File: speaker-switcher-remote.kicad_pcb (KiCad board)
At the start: 2 copper layers, 92 x 60 mm, 31 parts, among them M1 arduino-nano, Q1 2N2222, Q2 TIP31C, U1 LM7805_TO220

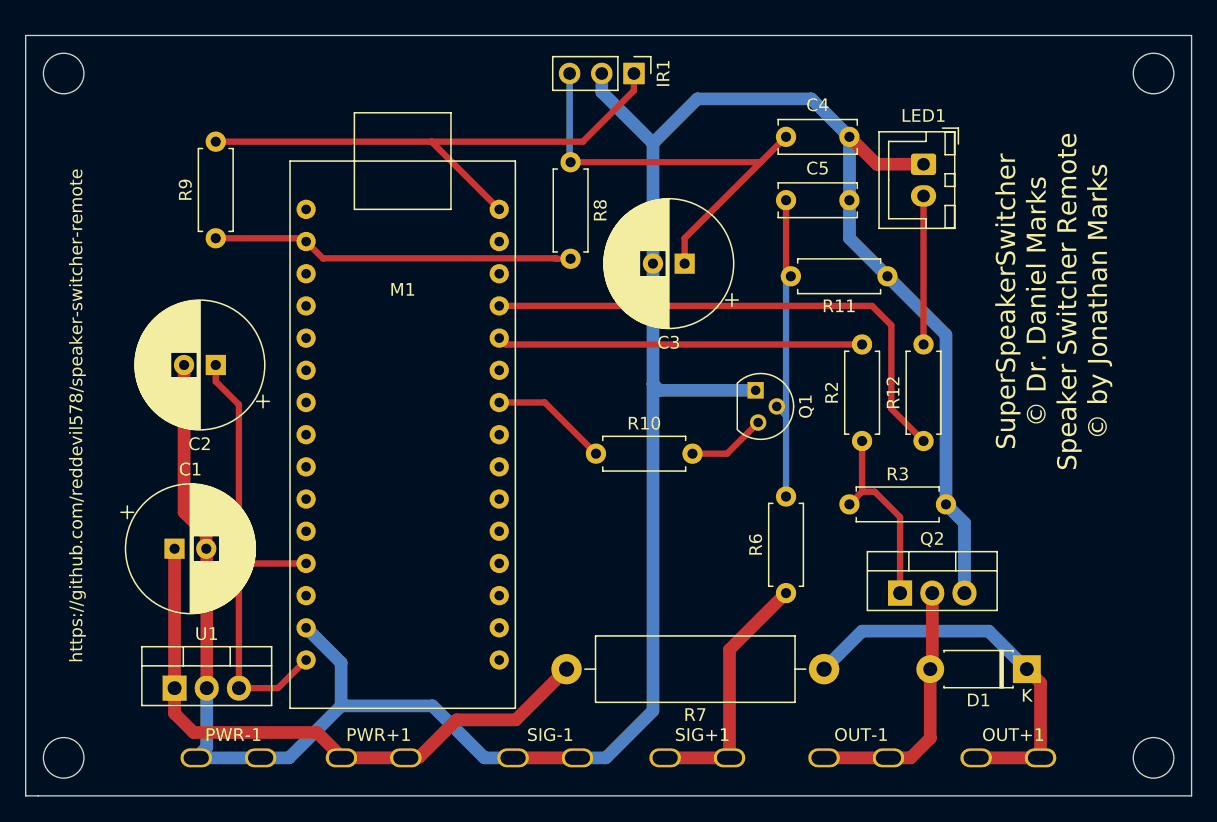
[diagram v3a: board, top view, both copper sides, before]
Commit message: Updated w/PNP output stage
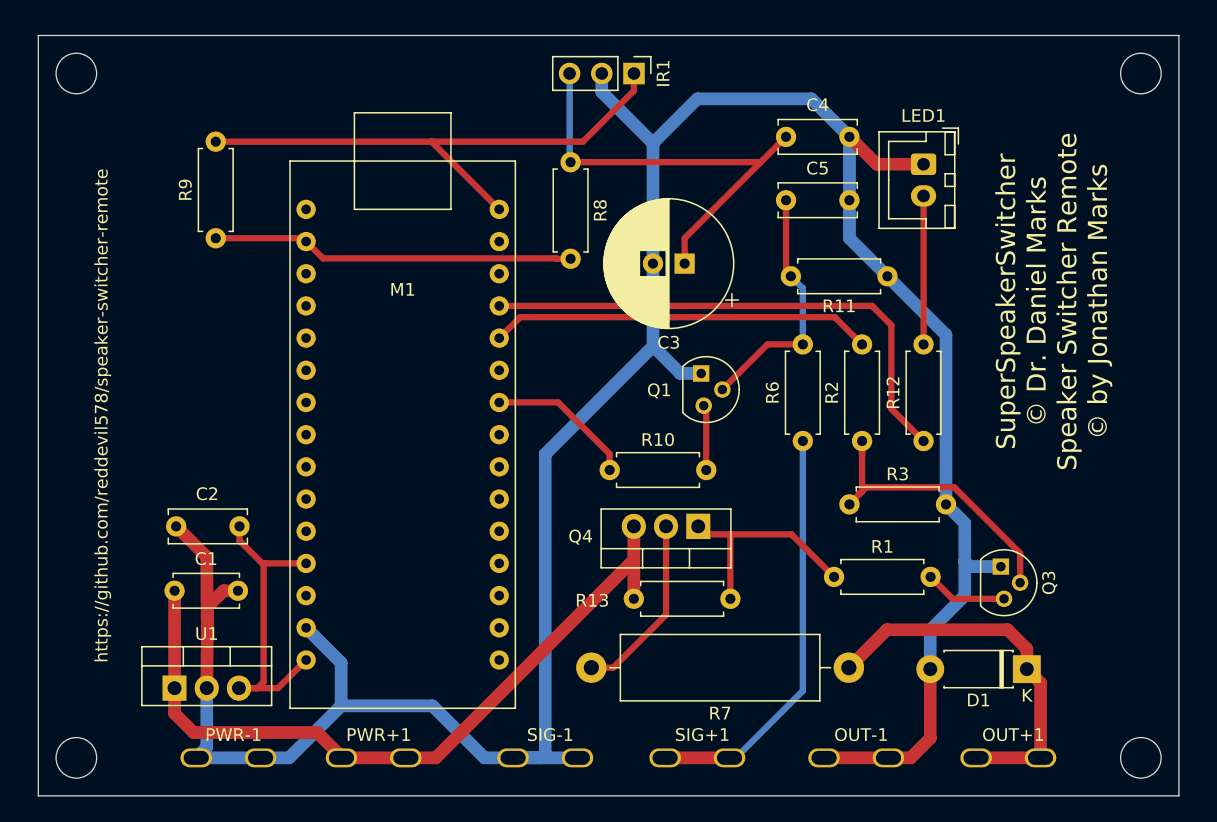
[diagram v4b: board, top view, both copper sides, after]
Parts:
- removed Q2: TIP31C, Package_TO_SOT_THT:TO-220-3_Vertical
- added Q3: 2N2222, Package_TO_SOT_THT:TO-92, F.Cu at (179.4, 110.4)
- added Q4: Q_PNP_BCE, Package_TO_SOT_THT:TO-220-3_Vertical, F.Cu at (155.3, 107.2)
- added R1: 2.2k, Resistor_THT:R_Axial_DIN0207_L6.3mm_D2.5mm_P7.62mm_Horizontal, F.Cu at (166.0, 111.2)
- added R13: 100k, Resistor_THT:R_Axial_DIN0207_L6.3mm_D2.5mm_P7.62mm_Horizontal, F.Cu at (150.2, 113.0)
- C1: footprint Capacitor_THT:CP_Radial_D10.0mm_P2.50mm -> Capacitor_THT:C_Disc_D5.0mm_W2.5mm_P5.00mm
- C2: footprint Capacitor_THT:CP_Radial_D10.0mm_P2.50mm -> Capacitor_THT:C_Disc_D6.0mm_W2.5mm_P5.00mm
- R12: value 150 -> 2.2k
- moved C2 12.9 mm to (119.1, 107.2)
- moved R6 12.1 mm to (163.6, 100.5)
- moved Q1 4.50 mm to (156.0, 95.2)
- moved C1 3.31 mm to (114.0, 112.3)
- moved R7 1.96 mm to (167.2, 118.4)
- moved R10 1.69 mm to (148.3, 102.8)
- moved REF** 1.00 mm to (106.2, 125.5)
- moved REF** 1.00 mm to (190.2, 125.5)
- moved REF** 1.00 mm to (190.2, 71.5)
- moved REF** 1.00 mm to (106.2, 71.5)
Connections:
- D1 pad 2: Net-(D1-Pad2) -> GNDREF
- M1 pad 1: Net-(M1-Pad1) -> (no net)
- M1 pad 10: Net-(M1-Pad10) -> (no net)
- M1 pad 11: Net-(M1-Pad11) -> (no net)
- M1 pad 13: Net-(M1-Pad13) -> (no net)
- M1 pad 17: Net-(M1-Pad17) -> (no net)
- M1 pad 18: Net-(M1-Pad18) -> (no net)
- M1 pad 21: Net-(M1-Pad21) -> (no net)
- M1 pad 23: Net-(M1-Pad23) -> (no net)
- M1 pad 24: Net-(M1-Pad24) -> (no net)
- M1 pad 25: Net-(M1-Pad25) -> (no net)
- M1 pad 26: Net-(M1-Pad26) -> (no net)
- M1 pad 27: Net-(M1-Pad27) -> (no net)
- M1 pad 28: Net-(M1-Pad28) -> (no net)
- M1 pad 29: Net-(M1-Pad29) -> (no net)
- M1 pad 3: Net-(M1-Pad3) -> (no net)
- M1 pad 30: Net-(M1-Pad30) -> (no net)
- M1 pad 4: Net-(M1-Pad4) -> (no net)
- M1 pad 5: Net-(M1-Pad5) -> (no net)
- M1 pad 6: Net-(M1-Pad6) -> (no net)
- M1 pad 7: Net-(M1-Pad7) -> (no net)
- M1 pad 8: Net-(M1-Pad8) -> (no net)
- M1 pad 9: Net-(M1-Pad9) -> (no net)
- OUT-1 pad 1: Net-(D1-Pad2) -> GNDREF
- R7 pad 2: PWR -> Net-(Q4-Pad2)
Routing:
- net Net-(D1-Pad2): track 20.5 -> 0.00 mm
- net Net-(Q4-Pad1): track 0.00 -> 17.2 mm
- net GNDREF: track 205.7 -> 222.0 mm
- net Net-(Q4-Pad2): track 0.00 -> 14.0 mm
- net /+5V: track 37.8 -> 24.8 mm
- net Net-(R6-Pad1): track 19.9 -> 32.8 mm
- net PWR: track 47.5 -> 59.1 mm
- net Net-(Q3-Pad2): track 15.2 -> 24.0 mm
- net Net-(Q3-Pad3): track 0.00 -> 6.51 mm
- net Net-(C5-Pad1): track 25.2 -> 19.8 mm
- net Net-(M1-Pad22): track 9.30 -> 11.7 mm
- net Net-(M1-Pad20): track 28.8 -> 30.2 mm
- net Net-(Q1-Pad3): track 6.20 -> 5.16 mm
- net Net-(D1-Pad1): track 31.0 -> 30.0 mm
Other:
- board size 92 x 60 mm -> 90 x 60 mm

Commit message: Rev 2.0
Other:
- board text added: "SuperSpeakerSwitcher © Dr. Daniel Marks Speaker Switcher Remote V2.0 © by Jonathan Marks"
- board text removed: "SuperSpeakerSwitcher © Dr. Daniel Marks Speaker Switcher Remote © by Jonathan Marks"
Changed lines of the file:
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@@
     (effects (font (size 1 1) (thickness 0.25)))
   )
-  (gr_text "SuperSpeakerSwitcher\n© Dr. Daniel Marks\nSpeaker Switcher Remote\n© by Jonathan Marks" (at 183.25 89.5 90) (layer F.SilkS)
+  (gr_text "SuperSpeakerSwitcher\n© Dr. Daniel Marks\nSpeaker Switcher Remote V2.0\n© by Jonathan Marks" (at 183.25 89.5 90) (layer F.SilkS)
     (effects (font (size 1.5 1.5) (thickness 0.3)))
   )
